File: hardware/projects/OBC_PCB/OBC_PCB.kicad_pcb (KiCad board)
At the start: 2 copper layers, 37 x 61 mm, 10 parts, among them J1 503566-2102, J2 DM3CS-SF, J3 USB4720-03-A, U1 MAX-M10S, U2 NPM1300-CAAA-R, U3 BMA400, U4 BMM350, U5 BMP581, U6 nRF54LM20A-PAXX

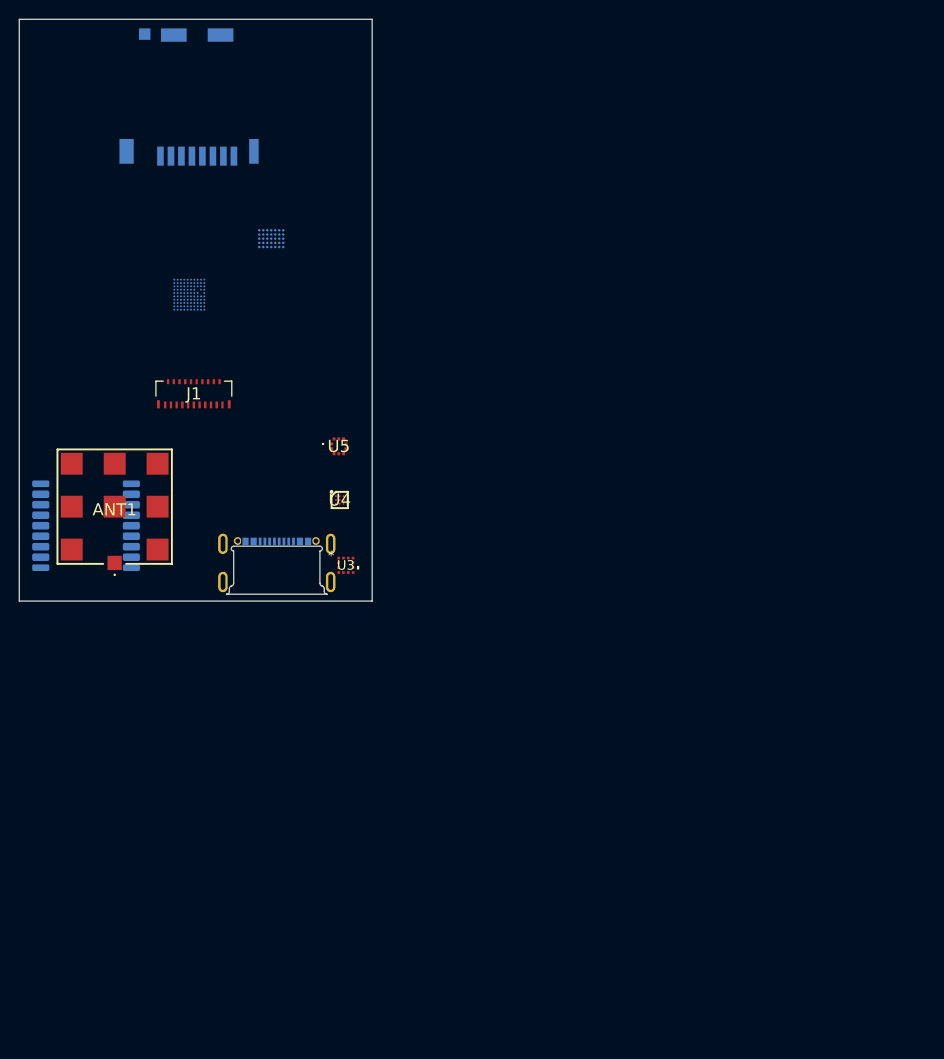
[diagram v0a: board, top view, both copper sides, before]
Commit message: hardware: place components on the enclosure outline and configure HDI rules
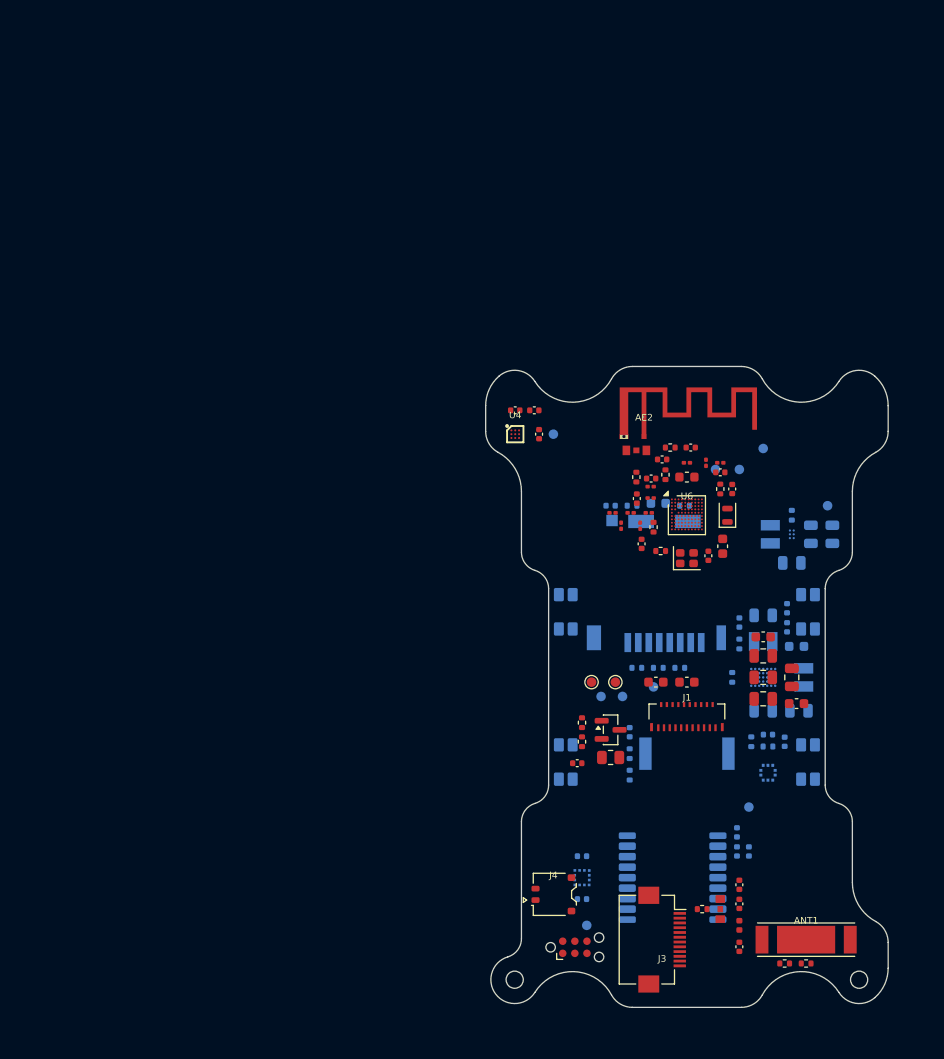
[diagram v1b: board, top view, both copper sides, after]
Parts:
- added AE2: PCB MIFA, RF_Antenna:Texas_SWRA117D_2.4GHz_Right, F.Cu at (95.5, 73.8)
- added BZ1: CPT-9019A-SMT-TR, obc:CPT-9019A-SMT-TR, B.Cu at (100.0, 107.0)
- added C1: 10u, Capacitor_SMD:C_0805_2012Metric, B.Cu at (108.0, 102.5)
- added C10: 10u, Capacitor_SMD:C_0805_2012Metric, B.Cu at (115.2, 84.0)
- added C11: 2.2u, Capacitor_SMD:C_0402_1005Metric, F.Cu at (102.2, 86.2)
- added C12: 4.7u, Capacitor_SMD:C_0201_0603Metric, F.Cu at (100.0, 76.5)
- added C13: 1p, Capacitor_SMD:C_0201_0603Metric, F.Cu at (96.2, 79.0)
- added C14: 1u, Capacitor_SMD:C_0603_1608Metric, F.Cu at (108.0, 94.8)
- added C15: 2.2u, Capacitor_SMD:C_0603_1608Metric, F.Cu at (111.5, 101.8)
- added C16: 100n, Capacitor_SMD:C_0402_1005Metric, B.Cu at (105.5, 93.2)
- added C17: 100n, Capacitor_SMD:C_0402_1005Metric, B.Cu at (110.5, 91.8)
- added C18: 10u, Capacitor_SMD:C_0805_2012Metric, F.Cu at (108.0, 96.8)
- added C19: 10u, Capacitor_SMD:C_0805_2012Metric, F.Cu at (111.0, 99.0)
- added C2: 10u, Capacitor_SMD:C_0805_2012Metric, B.Cu at (111.8, 102.5)
- added C20: 1u, Capacitor_SMD:C_0603_1608Metric, B.Cu at (111.5, 95.8)
- added C21: 10u, Capacitor_SMD:C_0402_1005Metric, F.Cu at (104.8, 79.2)
- added C22: 100n, Capacitor_SMD:C_0402_1005Metric, F.Cu at (94.8, 80.2)
- added C23: 100n, Capacitor_SMD:C_0402_1005Metric, F.Cu at (95.2, 85.0)
- added C24: 100n, Capacitor_SMD:C_0402_1005Metric, F.Cu at (96.2, 78.2)
- added C25: 2.2u, Capacitor_SMD:C_0201_0603Metric, F.Cu at (103.5, 76.5)
- added C26: 4.7u, Capacitor_SMD:C_0402_1005Metric, F.Cu at (103.5, 77.5)
- added C27: 10p, Capacitor_SMD:C_0402_1005Metric, F.Cu at (105.5, 127.2)
- added C28: 2.2u, Capacitor_SMD:C_0402_1005Metric, B.Cu at (105.2, 117.2)
- added C29: 100n, Capacitor_SMD:C_0402_1005Metric, B.Cu at (105.2, 115.2)
- added C3: 10u, Capacitor_SMD:C_0805_2012Metric, B.Cu at (108.0, 92.5)
- added C30: 100n, Capacitor_SMD:C_0402_1005Metric, B.Cu at (106.5, 117.2)
- added C31: 47p, Capacitor_SMD:C_0402_1005Metric, F.Cu at (105.5, 122.8)
- added C32: 4.3p, Capacitor_SMD:C_0402_1005Metric, F.Cu at (105.5, 120.8)
- added C33: 100n, Capacitor_SMD:C_0402_1005Metric, B.Cu at (89.0, 122.2)
- added C34: 100n, Capacitor_SMD:C_0402_1005Metric, B.Cu at (89.0, 117.8)
- added C35: 100n, Capacitor_SMD:C_0402_1005Metric, B.Cu at (110.2, 105.8)
- added C36: 100n, Capacitor_SMD:C_0402_1005Metric, B.Cu at (108.5, 105.0)
- added C37: 100n, Capacitor_SMD:C_0402_1005Metric, F.Cu at (82.0, 71.0)
- added C38: 100n, Capacitor_SMD:C_0402_1005Metric, F.Cu at (84.5, 73.5)
- added C39: 2.2u, Capacitor_SMD:C_0603_1608Metric, F.Cu at (100.0, 99.5)
- added C4: 10u, Capacitor_SMD:C_0805_2012Metric, F.Cu at (108.0, 99.0)
- added C40: 2.2u, Capacitor_SMD:C_0603_1608Metric, F.Cu at (96.8, 99.5)
- added C41: 10u, Capacitor_SMD:C_0603_1608Metric, B.Cu at (97.0, 80.8)
- added C42: 2.2u, Capacitor_SMD:C_0402_1005Metric, F.Cu at (84.0, 71.0)
- added C43: 100n, Capacitor_SMD:C_0402_1005Metric, B.Cu at (92.0, 81.0)
- added C44: 1u, Capacitor_SMD:C_0402_1005Metric, B.Cu at (94.0, 104.8)
- added C45: 1.2p, Capacitor_SMD:C_0201_0603Metric, F.Cu at (95.1, 83.1)
- added C46: 1.5p, Capacitor_SMD:C_0201_0603Metric, F.Cu at (93.1, 83.1)
- added C47: DNP, Capacitor_SMD:C_0402_1005Metric, F.Cu at (97.4, 76.2)
- added C48: DNP, Capacitor_SMD:C_0402_1005Metric, F.Cu at (100.4, 74.9)
- added C49: 1u, Capacitor_SMD:C_0402_1005Metric, F.Cu at (88.5, 108.0)
- added C5: 10u, Capacitor_SMD:C_0805_2012Metric, F.Cu at (108.0, 101.2)
- added C6: 1u, Capacitor_SMD:C_0603_1608Metric, F.Cu at (103.8, 85.2)
- added C7: 100n, Capacitor_SMD:C_0402_1005Metric, B.Cu at (110.5, 93.8)
- added C8: 10u, Capacitor_SMD:C_0805_2012Metric, B.Cu at (113.0, 84.0)
- added C9: 10u, Capacitor_SMD:C_0805_2012Metric, B.Cu at (111.0, 87.0)
- added H1: 1.8mm NPTH, , F.Cu at (81.9, 130.7)
- added H2: 1.8mm NPTH, , F.Cu at (118.1, 130.7)
- added H3: Cradle 4.2x1.6mm NPTH, , F.Cu at (89.0, 114.0)
- added H4: Cradle 4.2x1.6mm NPTH, , F.Cu at (89.0, 78.0)
- added H5: Cradle 4.2x1.6mm NPTH, , F.Cu at (111.0, 114.0)
- added H6: Cradle 4.2x1.6mm NPTH, , F.Cu at (111.0, 78.0)
- added J4: 1S Li-Po, obc:JST_ACH_2pin, F.Cu at (86.0, 121.8)
- added J5: TC2030-CTX-NL, Connector:Tag-Connect_TC2030-IDC-NL_2x03_P1.27mm_Vertical, F.Cu at (88.2, 127.3)
- added J7: RF coax pads, obc:RF_Coax_Solder_GSG, F.Cu at (94.7, 75.2)
- added J8: RF coax pads, obc:RF_Coax_Solder_GSG, F.Cu at (103.5, 123.3)
- added L1: 2.2uH, obc:Wurth_74404024022_2.5x2.0mm, B.Cu at (108.0, 95.2)
- added L10: 3.3nH, Inductor_SMD:L_0201_0603Metric, F.Cu at (92.2, 81.8)
- added L2: 2.2uH, obc:Wurth_74404024022_2.5x2.0mm, B.Cu at (112.2, 99.0)
- added L3: 4.7uH, Inductor_SMD:L_0603_1608Metric, F.Cu at (100.0, 78.0)
- added L4: 120R, Inductor_SMD:L_0201_0603Metric, F.Cu at (102.0, 76.5)
- added L5: 2.2uH, obc:Wurth_74404024022_2.5x2.0mm, B.Cu at (108.8, 84.0)
- added L6: 1.0nH, Inductor_SMD:L_0201_0603Metric, F.Cu at (96.2, 80.2)
- added L7: 3.9nH, Inductor_SMD:L_0402_1005Metric, F.Cu at (105.5, 125.0)
- added L8: 3.6nH, Inductor_SMD:L_0201_0603Metric, F.Cu at (96.0, 81.8)
- added L9: 4.7nH, Inductor_SMD:L_0201_0603Metric, F.Cu at (94.1, 81.8)
- added Q1: AO3400A, Package_TO_SOT_SMD:SOT-23, F.Cu at (92.0, 104.5)
- added R1: 0R, Resistor_SMD:R_0402_1005Metric, B.Cu at (104.8, 99.0)
- added R2: 150k, Resistor_SMD:R_0402_1005Metric, B.Cu at (105.5, 95.5)
- added R20: 10k, Resistor_SMD:R_0402_1005Metric, F.Cu at (97.8, 77.8)
- added R23: 4.7k, Resistor_SMD:R_0402_1005Metric, B.Cu at (108.5, 106.2)
- added R24: 4.7k, Resistor_SMD:R_0402_1005Metric, B.Cu at (106.8, 105.8)
- added R26: 0R, Resistor_SMD:R_0402_1005Metric, F.Cu at (112.5, 129.0)
- added R27: 0R, Resistor_SMD:R_0402_1005Metric, F.Cu at (110.2, 129.0)
- added R28: 47k, Resistor_SMD:R_0402_1005Metric, B.Cu at (94.2, 81.0)
- added R29: 47k, Resistor_SMD:R_0402_1005Metric, B.Cu at (99.8, 81.0)
- added R3: 1M, Resistor_SMD:R_0402_1005Metric, B.Cu at (111.0, 82.0)
- added R30: 47k, Resistor_SMD:R_0402_1005Metric, B.Cu at (97.0, 98.0)
- added R31: 47k, Resistor_SMD:R_0402_1005Metric, B.Cu at (94.8, 98.0)
- added R32: 47k, Resistor_SMD:R_0402_1005Metric, B.Cu at (99.2, 98.0)
- added R33: 1k, Resistor_SMD:R_0402_1005Metric, B.Cu at (94.0, 107.0)
- added R34: 100k, Resistor_SMD:R_0402_1005Metric, B.Cu at (94.0, 109.2)
- added R35: 0R, Resistor_SMD:R_0402_1005Metric, F.Cu at (98.2, 74.9)
- added R36: 220R, Resistor_SMD:R_0805_2012Metric, F.Cu at (92.0, 107.4)
- added R37: 1k, Resistor_SMD:R_0402_1005Metric, F.Cu at (89.0, 103.8)
- added R38: 100k, Resistor_SMD:R_0402_1005Metric, F.Cu at (89.0, 105.8)
- added R39: 0R, Resistor_SMD:R_0402_1005Metric, F.Cu at (94.7, 78.0)
- added R4: 200R, Resistor_SMD:R_0402_1005Metric, F.Cu at (96.5, 83.2)
- added R40: 0R, Resistor_SMD:R_0402_1005Metric, F.Cu at (101.6, 123.3)
- added R5: 2.2R, Resistor_SMD:R_0402_1005Metric, F.Cu at (103.5, 79.2)
- added R9: 33R, Resistor_SMD:R_0402_1005Metric, F.Cu at (97.2, 85.8)
- added SW1: PREV, obc:TL1016AAF220QG, B.Cu at (87.3, 92.1)
- added SW2: NEXT, obc:TL1016AAF220QG, B.Cu at (87.3, 107.9)
- added SW3: SELECT / POWER, obc:TL1016AAF220QG, B.Cu at (112.7, 92.1)
- added SW4: BACK, obc:TL1016AAF220QG, B.Cu at (112.7, 107.9)
- added TP1: SHPHLD, TestPoint:TestPoint_Pad_D1.0mm, B.Cu at (91.0, 101.0)
- added TP10: +5V_DISP, TestPoint:TestPoint_Pad_D1.0mm, B.Cu at (114.8, 81.0)
- added TP11: SCL, TestPoint:TestPoint_Pad_D1.0mm, F.Cu at (90.0, 99.5)
- added TP12: SDA, TestPoint:TestPoint_Pad_D1.0mm, F.Cu at (92.5, 99.5)
- added TP2: SAFEBOOT, TestPoint:TestPoint_Pad_D1.0mm, B.Cu at (93.2, 101.0)
- added TP3: VBAT, TestPoint:TestPoint_Pad_D1.0mm, B.Cu at (89.5, 125.0)
- added TP4: VSYS, TestPoint:TestPoint_Pad_D1.0mm, B.Cu at (108.0, 75.0)
- added TP5: +3V2, TestPoint:TestPoint_Pad_D1.0mm, B.Cu at (103.0, 77.2)
- added TP6: GND, TestPoint:TestPoint_Pad_D1.0mm, B.Cu at (105.5, 77.2)
- added TP7: +3V2_GPS, TestPoint:TestPoint_Pad_D1.0mm, B.Cu at (106.5, 112.6)
- added TP8: +3V3_SD, TestPoint:TestPoint_Pad_D1.0mm, B.Cu at (96.5, 100.0)
- added TP9: +1V8_MAG, TestPoint:TestPoint_Pad_D1.0mm, B.Cu at (86.0, 73.5)
- added U7: TPS610997, obc:TI_YFF0006_0.884x1.226mm_P0.4mm, B.Cu at (111.0, 84.0)
- added Y1: 32MHz, Crystal:Crystal_SMD_2016-4Pin_2.0x1.6mm, F.Cu at (100.0, 86.5)
- added Y3: 32.768kHz, Crystal:Crystal_SMD_2012-2Pin_2.0x1.2mm, F.Cu at (104.2, 82.0)
- ANT1: value SGGP.12.4.A.02 -> GGBLA.125.A; footprint obc:SGGP124A02 -> obc:Taoglas_GGBLA125A_10x3.2mm_ContactPads
- J1: value 503566-2102 -> LS021B7DD02
- J3: value USB4720-03-A -> FH12-12S-0.5SH(55); footprint obc:GCT_USB4720-03-A_REVA -> Connector_FFC-FPC:Hirose_FH12-12S-0.5SH_1x12-1MP_P0.50mm_Horizontal; moved to F.Cu
- U1: value MAX-M10S -> MAX-F11N; footprint RF_GPS:ublox_MAX -> obc:ublox_MAX_F11N_Provisional
- U3, U5: moved to B.Cu
- U6: value nRF54LM20A-PAXX -> nRF54LM20A-PAAA; moved to F.Cu
- moved ANT1 85.5 mm to (112.5, 126.5)
- moved U1 71.7 mm to (98.5, 120.0), turned to 0 degrees
- moved J2 70.7 mm to (97.0, 89.0)
- moved U2 69.1 mm to (108.0, 99.0), turned to 0 degrees
- moved J1 61.8 mm to (100.0, 103.1)
- moved U6 57.0 mm to (100.0, 82.0), turned to 0 degrees
- moved U5 56.5 mm to (108.5, 109.0)
- moved J3 55.1 mm to (97.4, 126.5), turned to -90 degrees
- moved U3 41.1 mm to (89.0, 120.0)
- moved U4 19.7 mm to (82.0, 73.5)
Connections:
- ANT1 pad 1: unconnected-(ANT1-RF_FEED-Pad1) -> Net-(ANT1-~)
- ANT1 pad 2: unconnected-(ANT1-GND-Pad2) -> Net-(ANT1-FTE-Pad2)
- ANT1 pad 3: unconnected-(ANT1-GND-Pad3) -> Net-(ANT1-FTE-Pad3)
- J1 pad 1: unconnected-(J1-Pad1) -> +5V_DISP
- J1 pad 10: unconnected-(J1-Pad10) -> GND
- J1 pad 11: unconnected-(J1-Pad11) -> /Display/LCD.BSP
- J1 pad 12: unconnected-(J1-Pad12) -> /Display/FLPR.P07
- J1 pad 13: unconnected-(J1-Pad13) -> /FLPR.P00
- J1 pad 14: unconnected-(J1-Pad14) -> /FLPR.P04
- J1 pad 15: unconnected-(J1-Pad15) -> /Display/FLPR.P06
- J1 pad 16: unconnected-(J1-Pad16) -> /Display/FLPR.P08
- J1 pad 17: unconnected-(J1-Pad17) -> /Display/FLPR.P09
- J1 pad 18: unconnected-(J1-Pad18) -> /Display/FLPR.P10
- J1 pad 20: unconnected-(J1-Pad20) -> /Display/LCD.VCOM
- J1 pad 3: unconnected-(J1-Pad3) -> /Display/LCD.GSP
- J1 pad 4: unconnected-(J1-Pad4) -> /Display/LCD.GCK
- J1 pad 5: unconnected-(J1-Pad5) -> /Display/LCD.GEN
- J1 pad 6: unconnected-(J1-Pad6) -> /Display/LCD.INTB
- J1 pad 7: unconnected-(J1-Pad7) -> /Display/LCD.VB
- J1 pad 8: unconnected-(J1-Pad8) -> /Display/LCD.VA
- J1 pad 9: unconnected-(J1-Pad9) -> +3V2
- J2 pad 1: unconnected-(J2-DAT2-Pad1) -> /Display/FLPR.P03
- J2 pad 2: unconnected-(J2-CD/DAT3-Pad2) -> /FLPR.P00
- J2 pad 3: unconnected-(J2-CMD-Pad3) -> /Display/FLPR.P05
- J2 pad 4: unconnected-(J2-VDD-Pad4) -> +3V3_SD
- J2 pad 5: unconnected-(J2-CLK-Pad5) -> /Display/FLPR.P01
- J2 pad 6: unconnected-(J2-VSS-Pad6) -> GND
- J2 pad 7: unconnected-(J2-DAT0-Pad7) -> /Display/FLPR.P02
- J2 pad 8: unconnected-(J2-DAT1-Pad8) -> /FLPR.P04
- J2 pad S1: unconnected-(J2-GND-PadS1) -> GND
- J2 pad S2: unconnected-(J2-GND-PadS2) -> GND
- J2 pad S3: unconnected-(J2-GND-PadS3) -> GND
- J2 pad S5: unconnected-(J2-GND-PadS5) -> GND
- U1 pad 1: Net-(U1-GND-Pad1) -> GND
- U1 pad 10: Net-(U1-GND-Pad1) -> GND
- U1 pad 11: unconnected-(U1-RF_IN-Pad11) -> Net-(U1-RF_IN)
- U1 pad 12: Net-(U1-GND-Pad1) -> GND
- U1 pad 18: unconnected-(U1-~{SAFEBOOT}-Pad18) -> Net-(U1-~{SAFEBOOT})
- U1 pad 2: unconnected-(U1-TXD-Pad2) -> /GPS_TXD
- U1 pad 3: unconnected-(U1-RXD-Pad3) -> /GPS_RXD
- U1 pad 6: unconnected-(U1-V_BCKP-Pad6) -> +3V2
- U1 pad 7: unconnected-(U1-VCC_IO-Pad7) -> +3V2_GPS
- U1 pad 8: unconnected-(U1-VCC-Pad8) -> +3V2_GPS
- U2 pad A4: unconnected-(U2-LSOUT1/VOUTLDO1-PadA4) -> +1V8_MAG
- U2 pad A5: unconnected-(U2-LSOUT2/VOUTLDO2-PadA5) -> +3V2_GPS
- U2 pad A6: unconnected-(U2-AVSS-PadA6) -> GND
- U2 pad A7: unconnected-(U2-PVSS1-PadA7) -> GND
- U2 pad B1: unconnected-(U2-VBUS-PadB1) -> VBUS
- U2 pad B2: unconnected-(U2-VBUS-PadB2) -> VBUS
- U2 pad B3: unconnected-(U2-CC2-PadB3) -> /Power Management/USB_CC2
- U2 pad B4: unconnected-(U2-LSIN1/VINLDO1-PadB4) -> +3V2
- U2 pad B5: unconnected-(U2-LSIN2/VINLDO2-PadB5) -> +3V2
- U2 pad B6: unconnected-(U2-VOUT1-PadB6) -> +3V3_SD
- U2 pad B7: unconnected-(U2-SW1-PadB7) -> Net-(U2-SW1)
- U2 pad C1: unconnected-(U2-VSYS-PadC1) -> VSYS
- U2 pad C2: unconnected-(U2-VSYS-PadC2) -> VSYS
- U2 pad C3: unconnected-(U2-VBUSOUT-PadC3) -> USB_VBUS
- U2 pad C6: unconnected-(U2-VOUT2-PadC6) -> +3V2
- U2 pad C7: unconnected-(U2-PVDD-PadC7) -> VSYS
- U2 pad D1: unconnected-(U2-VBAT-PadD1) -> VBAT
- U2 pad D2: unconnected-(U2-VBAT-PadD2) -> VBAT
- U2 pad D3: unconnected-(U2-NTC-PadD3) -> GND
- U2 pad D4: unconnected-(U2-SHPHLD-PadD4) -> /Power Management/SHPHLD
- U2 pad D5: unconnected-(U2-CC1-PadD5) -> /Power Management/USB_CC1
- U2 pad D7: unconnected-(U2-SW2-PadD7) -> Net-(U2-SW2)
- U2 pad E1: unconnected-(U2-VSET2-PadE1) -> Net-(U2-VSET2)
- U2 pad E2: unconnected-(U2-VSET1-PadE2) -> Net-(U2-VSET1)
- U2 pad E3: unconnected-(U2-SCL-PadE3) -> SCL
- U2 pad E4: unconnected-(U2-VDDIO-PadE4) -> +3V2
- U2 pad E5: unconnected-(U2-SDA-PadE5) -> SDA
- U2 pad E6: unconnected-(U2-GPIO1-PadE6) -> PMIC_INT
- U2 pad E7: unconnected-(U2-PVSS2-PadE7) -> GND
- U3 pad 1: unconnected-(U3-SDO-Pad1) -> GND
- U3 pad 10: unconnected-(U3-CSB-Pad10) -> +3V2
- U3 pad 12: unconnected-(U3-SCX-Pad12) -> SCL
- U3 pad 2: unconnected-(U3-SDX-Pad2) -> SDA
- U3 pad 3: unconnected-(U3-VDDIO-Pad3) -> +3V2
- U3 pad 5: unconnected-(U3-INT1-Pad5) -> /ACC_INT1
- U3 pad 7: unconnected-(U3-VDD-Pad7) -> +3V2
- U3 pad 8: unconnected-(U3-GNDIO-Pad8) -> GND
- U3 pad 9: unconnected-(U3-GND-Pad9) -> GND
- U4 pad A2: unconnected-(U4-SDA-PadA2) -> SDA
- U4 pad A3: unconnected-(U4-SCK-PadA3) -> SCL
- U4 pad B1: unconnected-(U4-GND-PadB1) -> GND
- U4 pad B2: unconnected-(U4-ADSEL-PadB2) -> +3V2
- U4 pad B3: unconnected-(U4-VDDIO-PadB3) -> +3V2
- U4 pad C1: unconnected-(U4-VDD-PadC1) -> +1V8_MAG
- U4 pad C2: unconnected-(U4-CRST-PadC2) -> Net-(U4-CRST)
- U4 pad C3: unconnected-(U4-BYPASS-PadC3) -> GND
- U5 pad 1: unconnected-(U5-VDDIO-Pad1) -> +3V2
- U5 pad 10: unconnected-(U5-VDD-Pad10) -> +3V2
- U5 pad 2: unconnected-(U5-SCK-Pad2) -> SCL
- U5 pad 3: unconnected-(U5-VSS-Pad3) -> GND
- U5 pad 4: unconnected-(U5-SDI-Pad4) -> SDA
- U5 pad 5: unconnected-(U5-SDO-Pad5) -> +3V2
- U5 pad 6: unconnected-(U5-CSB-Pad6) -> +3V2
- U5 pad 7: unconnected-(U5-INT-Pad7) -> GND
- U5 pad 8: unconnected-(U5-VSS-Pad8) -> GND
- U5 pad 9: unconnected-(U5-VSS-Pad9) -> GND
- U6 pad A1: Net-(U6A-VSS-PadA1) -> GND
- U6 pad A10: Net-(U6A-VSS-PadA1) -> GND
- U6 pad A2: unconnected-(U6A-XC1-PadA2) -> Net-(U6A-XC1)
- U6 pad A3: Net-(U6A-VDD-PadA3) -> +3V2
- U6 pad A4: Net-(U6A-VDD-PadA3) -> +3V2
- U6 pad A5: unconnected-(U6A-DCC-PadA5) -> Net-(U6A-DCC)
- U6 pad A6: unconnected-(U6A-DECD-PadA6) -> Net-(U6A-DECD)
- U6 pad A7: Net-(U6A-VSS-PadA1) -> GND
- U6 pad A8: unconnected-(U6A-DECA-PadA8) -> Net-(U6A-DECA)
- U6 pad A9: Net-(U6A-VDD-PadA3) -> +3V2
- U6 pad B1: unconnected-(U6A-XC2-PadB1) -> Net-(U6A-XC2)
- U6 pad B10: unconnected-(U6D-P2.00-PadB10) -> /FLPR.P00
- U6 pad B2: unconnected-(U6C-P1.15-PadB2) -> /Display/LCD.VCOM
- U6 pad B3: unconnected-(U6C-P1.16-PadB3) -> /Display/LCD.VB
- U6 pad B4: unconnected-(U6C-P1.17-PadB4) -> /Display/LCD.VA
- U6 pad B9: unconnected-(U6D-P2.06-PadB9) -> /Display/FLPR.P06
- U6 pad C1: unconnected-(U6A-DECRF-PadC1) -> Net-(U6A-DECRF)
- U6 pad C10: unconnected-(U6D-P2.01-PadC10) -> Net-(U6D-P2.01)
- U6 pad C2: unconnected-(U6C-P1.14-PadC2) -> /Display/LCD.BSP
- U6 pad C3: unconnected-(U6C-P1.13-PadC3) -> /Display/LCD.INTB
- U6 pad C4: unconnected-(U6C-P1.12-PadC4) -> /Display/LCD.GEN
- U6 pad C5: unconnected-(U6C-P1.11-PadC5) -> /Display/LCD.GCK
- U6 pad C6: unconnected-(U6A-P1.20-PadC6) -> Net-(U6A-P1.20)
- U6 pad C7: unconnected-(U6A-P1.21-PadC7) -> Net-(U6A-P1.21)
- U6 pad C9: unconnected-(U6D-P2.07-PadC9) -> /Display/FLPR.P07
- U6 pad D1: Net-(U6A-VSS-PadA1) -> GND
- U6 pad D10: unconnected-(U6D-P2.02-PadD10) -> /Display/FLPR.P02
- U6 pad D2: Net-(U6A-VSS-PadA1) -> GND
- U6 pad D4: unconnected-(U6E-P3.12-PadD4) -> Net-(U6E-P3.12)
- U6 pad D5: unconnected-(U6C-P1.10-PadD5) -> /Display/LCD.GSP
- U6 pad D9: unconnected-(U6D-P2.08-PadD9) -> /Display/FLPR.P08
- U6 pad E1: unconnected-(U6A-ANT-PadE1) -> /Radio/ANT
- U6 pad E10: unconnected-(U6D-P2.03-PadE10) -> /Display/FLPR.P03
- U6 pad E3: unconnected-(U6B-P0.09-PadE3) -> /GPS_RXD
- U6 pad E4: unconnected-(U6E-P3.11-PadE4) -> /BACKLIGHT_PWM
- U6 pad E5: Net-(U6A-VSS-PadA1) -> GND
- U6 pad E6: Net-(U6A-VSS-PadA1) -> GND
- U6 pad E9: unconnected-(U6D-P2.09-PadE9) -> /Display/FLPR.P09
- U6 pad F1: Net-(U6A-VSS-PadA1) -> GND
- U6 pad F10: unconnected-(U6D-P2.04-PadF10) -> /FLPR.P04
- U6 pad F2: unconnected-(U6A-~{RESET}-PadF2) -> /nRESET
- U6 pad F3: unconnected-(U6B-P0.08-PadF3) -> PMIC_INT
- U6 pad F5: Net-(U6A-VSS-PadA1) -> GND
- U6 pad F6: Net-(U6A-VSS-PadA1) -> GND
- U6 pad F7: unconnected-(U6E-P3.09-PadF7) -> DISP_5V_EN
- U6 pad F9: unconnected-(U6D-P2.10-PadF9) -> /Display/FLPR.P10
- U6 pad G1: unconnected-(U6A-SWDCLK-PadG1) -> /SWDCLK
- U6 pad G10: Net-(U6A-VDD-PadA3) -> +3V2
- U6 pad G2: unconnected-(U6A-SWDIO-PadG2) -> /SWDIO
- U6 pad G3: unconnected-(U6B-P0.07-PadG3) -> /BTN_BACK
- U6 pad G9: unconnected-(U6D-P2.05-PadG9) -> /Display/FLPR.P05
- U6 pad H1: Net-(U6A-VDD-PadA3) -> +3V2
- U6 pad H2: unconnected-(U6B-P0.06-PadH2) -> /BTN_NEXT
- U6 pad H3: unconnected-(U6B-P0.05-PadH3) -> /BTN_PREV
- U6 pad J2: unconnected-(U6B-P0.03-PadJ2) -> /GPS_TXD
- U6 pad J3: unconnected-(U6B-P0.02-PadJ3) -> SCL
- U6 pad J5: unconnected-(U6A-TXRTUNE-PadJ5) -> Net-(U6A-TXRTUNE)
- U6 pad K1: Net-(U6A-VSS-PadA1) -> GND
- U6 pad K10: Net-(U6A-VSS-PadA1) -> GND
- U6 pad K2: unconnected-(U6B-P0.01-PadK2) -> SDA
- U6 pad K3: unconnected-(U6B-P0.00-PadK3) -> /ACC_INT1
- U6 pad K4: unconnected-(U6A-D--PadK4) -> /Power Management/USB_D-
- U6 pad K5: unconnected-(U6A-D+-PadK5) -> /Power Management/USB_D+
- U6 pad K6: unconnected-(U6A-DECUSB-PadK6) -> Net-(U6A-DECUSB)
- U6 pad K7: unconnected-(U6A-VBUS-PadK7) -> Net-(U6A-VBUS)
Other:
- board size 37 x 61 mm -> 42.2 x 67.2 mm
- copper layers 2 -> 8
- board text added: "BACKLIGHT: Q1/R36-R38/C49 placed; J6 connector/tail footprint TBD."
- board text added: "BMM350: Bosch guide 3.9 says no ENIG. Confirm compatible PCB finish before fabrication."
- board text added: "CRADLE: H3-H6, 4.2x1.6 NPTH; front supports + release access reserved"
- board text added: "DISPLAY + FLEX PROJECTION"
- board text added: "HDI: tentative 3+2+3; filled/capped microvias. U6 land size needs fab approval. RF 50-ohm / USB 90-ohm: width and gap pending stackup. Green mask >= 0.102mm web."
- board text added: "J5: TC2030-CTX-NL. No paste. Keep 0.508mm from other tracks; clear probe access."
- board text added: "PCBWay HDI / 8 layers / 1.6mm target. Confirm stackup and 0.35mm CSP escape."
- board text added: "PLACEMENT DRAFT - UNROUTED"
- board text added: "RF TEST: remove R39 (BLE) or R40 (GNSS). Center pad in feed; no branch stub."
- board text added: "Rough placement only; battery and RF stackup not finalized."
- board text added: "USB + BATTERY: front access below display. Backlight connector pending."

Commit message: hardware: complete first main-board routing pass
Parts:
- removed C44: 1u, Capacitor_SMD:C_0402_1005Metric
- removed R34: 100k, Resistor_SMD:R_0402_1005Metric
- added C50: DNP, Capacitor_SMD:C_0402_1005Metric, B.Cu at (104.9, 116.2)
- added R41: 470R, Resistor_SMD:R_0402_1005Metric, B.Cu at (94.0, 109.2)
- added TP13: USB_VBUS, TestPoint:TestPoint_Pad_D1.0mm, F.Cu at (110.0, 104.0)
- ANT1: footprint obc:Taoglas_GGBLA125A_10x3.2mm_ContactPads -> obc:Taoglas_GGBLA125A_10x3.2mm_Corner
- C12, C13, C25, C45, C46: footprint Capacitor_SMD:C_0201_0603Metric -> obc:C_Nordic_0201_0603Metric
- C27, C31, C32, L7: moved to B.Cu
- L10, L4, L6, L8, L9: footprint Inductor_SMD:L_0201_0603Metric -> obc:L_Nordic_0201_0603Metric
- R33: value 1k -> 470R
- moved C30 14.9 mm to (91.7, 118.9), turned to 180 degrees
- moved C29 13.8 mm to (91.7, 117.8), turned to 180 degrees
- moved C28 13.6 mm to (91.7, 116.7), turned to 180 degrees
- moved C27 12.5 mm to (111.0, 116.0), turned to 0 degrees
- moved R27 12.0 mm to (105.3, 118.0), turned to 90 degrees
- moved L7 11.3 mm to (113.1, 116.6)
- moved J8 11.2 mm to (106.3, 112.5), turned to 90 degrees
- moved C26 11.0 mm to (102.9, 88.5), turned to -90 degrees
- moved R40 9.80 mm to (106.3, 114.7), turned to 90 degrees
- moved C25 9.66 mm to (96.5, 83.1), turned to -90 degrees
- moved C23 9.60 mm to (104.8, 86.0), turned to -90 degrees
- moved R5 9.28 mm to (104.3, 88.5)
- moved R9 9.04 mm to (106.2, 87.0)
- moved R4 8.72 mm to (101.2, 90.6)
- moved C20 8.11 mm to (105.5, 101.2)
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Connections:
- net PMIC_INT renamed /PMIC_INT
- net USB_VBUS renamed /USB_VBUS
- BZ1 pad 2: GND -> Net-(BZ1-~-Pad2)
- J3 pad 1: VBUS -> GND
- J3 pad 10: /Power Management/USB_CC2 -> VBUS
- J3 pad 11: GND -> VBUS
- J3 pad 4: VBUS -> /Power Management/USB_CC1
- J3 pad 5: /Power Management/USB_CC1 -> GND
- J3 pad 6: GND -> /Power Management/USB_D+
- J3 pad 7: /Power Management/USB_D+ -> /Power Management/USB_D-
- J3 pad 8: /Power Management/USB_D- -> GND
- J3 pad 9: GND -> /Power Management/USB_CC2
- R23 pad 2: SDA -> /SDA
- R24 pad 2: SCL -> /SCL
- R3 pad 1: DISP_5V_EN -> /DISP_5V_EN
- R33 pad 1: Net-(U6E-P3.12) -> /PIEZO_A
- R33 pad 2: Net-(C44-Pad1) -> Net-(BZ1-~-Pad1)
- TP11 pad 1: SCL -> /SCL
- TP12 pad 1: SDA -> /SDA
- U2 pad E3: SCL -> /SCL
- U2 pad E5: SDA -> /SDA
- U3 pad 12: SCL -> /SCL
- U3 pad 2: SDA -> /SDA
- U4 pad A2: SDA -> /SDA
- U4 pad A3: SCL -> /SCL
- U5 pad 2: SCL -> /SCL
- U5 pad 4: SDA -> /SDA
- U5 pad 7: GND -> /BARO_INT
- U6 pad C5: /Display/LCD.GCK -> unconnected-(U6C-P1.11-PadC5)
- U6 pad D4: Net-(U6E-P3.12) -> unconnected-(U6E-P3.12-PadD4)
- U6 pad E4: /BACKLIGHT_PWM -> unconnected-(U6E-P3.11-PadE4)
- U6 pad F7: DISP_5V_EN -> unconnected-(U6E-P3.09-PadF7)
- U6 pad H10: unconnected-(U6C-P1.29-PadH10) -> /DISP_5V_EN
- U6 pad H8: unconnected-(U6C-P1.05-PadH8) -> /Display/LCD.GCK
- U6 pad H9: unconnected-(U6C-P1.03-PadH9) -> /SCL
- U6 pad J10: unconnected-(U6C-P1.30-PadJ10) -> /BACKLIGHT_PWM
- U6 pad J3: SCL -> unconnected-(U6B-P0.02-PadJ3)
- U6 pad J9: unconnected-(U6C-P1.04-PadJ9) -> /SDA
- U6 pad K2: SDA -> /BARO_INT
- U6 pad K8: unconnected-(U6C-P1.00-PadK8) -> /PIEZO_B
- U6 pad K9: unconnected-(U6C-P1.31-PadK9) -> /PIEZO_A
- U7 pad C1: DISP_5V_EN -> /DISP_5V_EN
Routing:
- net /SDA: track 0.00 -> 113.0 mm, vias 0 -> 15
- net /SCL: track 0.00 -> 102.4 mm, vias 0 -> 14
- net +3V3_SD: track 0.00 -> 70.5 mm, vias 0 -> 9
- net /nRESET: track 0.00 -> 67.8 mm, vias 0 -> 5
- net +1V8_MAG: track 0.00 -> 66.0 mm, vias 0 -> 11
- net VBAT: track 0.00 -> 62.6 mm, vias 0 -> 3
- net /PIEZO_A: track 0.00 -> 55.6 mm, vias 0 -> 7
- net +5V_DISP: track 0.00 -> 54.6 mm, vias 0 -> 3
- net /GPS_RXD: track 0.00 -> 51.4 mm, vias 0 -> 3
- net +3V2: track 0.00 -> 50.0 mm, vias 0 -> 48
- net /SWDIO: track 0.00 -> 49.9 mm, vias 0 -> 3
- net /SWDCLK: track 0.00 -> 49.2 mm, vias 0 -> 3
- net /BACKLIGHT_PWM: track 0.00 -> 48.0 mm, vias 0 -> 9
- net /Display/FLPR.P06: track 0.00 -> 47.4 mm, vias 0 -> 4
- net +3V2_GPS: track 0.00 -> 46.0 mm, vias 0 -> 4
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- added copper zone on In3.Cu, net +3V2
- added copper zone on B.Cu, net GND
- added copper zone on F.Cu, net GND
- added copper zone on In1.Cu, net GND
- added copper zone on In4.Cu, net GND
- added copper zone on In6.Cu, net GND

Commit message: hardware: rework main-board routing after layout review
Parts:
- added FID1: Fiducial_1mm_Mask2mm, Fiducial:Fiducial_1mm_Mask2mm, F.Cu at (85.2, 80.5)
- added FID10: Fiducial_0.5mm_Mask1mm, Fiducial:Fiducial_0.5mm_Mask1mm, B.Cu at (110.0, 110.0)
- added FID2: Fiducial_1mm_Mask2mm, Fiducial:Fiducial_1mm_Mask2mm, F.Cu at (114.8, 85.5)
- added FID3: Fiducial_1mm_Mask2mm, Fiducial:Fiducial_1mm_Mask2mm, F.Cu at (95.0, 119.0)
- added FID4: Fiducial_1mm_Mask2mm, Fiducial:Fiducial_1mm_Mask2mm, B.Cu at (85.2, 80.5)
- added FID5: Fiducial_1mm_Mask2mm, Fiducial:Fiducial_1mm_Mask2mm, B.Cu at (107.0, 81.0)
- added FID6: Fiducial_1mm_Mask2mm, Fiducial:Fiducial_1mm_Mask2mm, B.Cu at (85.8, 124.5)
- added FID7: Fiducial_0.5mm_Mask1mm, Fiducial:Fiducial_0.5mm_Mask1mm, F.Cu at (97.2, 89.2)
- added FID8: Fiducial_0.5mm_Mask1mm, Fiducial:Fiducial_0.5mm_Mask1mm, F.Cu at (105.8, 80.8)
- added FID9: Fiducial_0.5mm_Mask1mm, Fiducial:Fiducial_0.5mm_Mask1mm, B.Cu at (106.8, 110.6)
- C14, C15, C18, C19, C4, C5, J8, R40: moved to B.Cu
- R33, R41: moved to F.Cu
- moved C35 32.5 mm to (87.2, 82.8), turned to 0 degrees
- moved U5 31.7 mm to (87.2, 85.5)
- moved TP4 27.2 mm to (101.1, 101.3)
- moved C36 27.1 mm to (87.2, 88.2)
- moved R41 22.9 mm to (102.2, 87.8), turned to -90 degrees
- moved R33 21.5 mm to (104.0, 88.0), turned to -90 degrees
- moved C43 17.6 mm to (99.0, 97.2)
- moved C41 17.4 mm to (97.1, 98.1), turned to -90 degrees
- moved TP7 16.1 mm to (90.6, 110.0), turned to 180 degrees
- moved BZ1 16.0 mm to (99.0, 123.0)
- moved TP2 14.8 mm to (94.0, 115.8)
- moved C28 12.8 mm to (90.5, 104.0)
- moved C29 12.3 mm to (90.5, 105.6)
- moved U1 12.0 mm to (98.0, 108.0)
- moved C30 11.8 mm to (90.5, 107.2)
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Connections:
- net Net-(AE2-FEED) renamed /Radio/RF24_FEED
- net Net-(ANT1-FTE-Pad2) renamed /GNSS/GNSS_FTE1
- net Net-(ANT1-FTE-Pad3) renamed /GNSS/GNSS_FTE2
- net Net-(ANT1-~) renamed /GNSS/GNSS_RF_FEED
- net Net-(C27-Pad1) renamed /GNSS/GNSS_RF_MATCH
- net Net-(C45-Pad1) renamed /Radio/RF24_M1
- net Net-(C46-Pad1) renamed /Radio/RF24_M2
- net Net-(J7-In) renamed /Radio/RF24_TEST
- net Net-(J8-In) renamed /GNSS/GNSS_RF_TEST
- net Net-(L10-Pad2) renamed /Radio/RF24_LPF
- net Net-(U1-RF_IN) renamed /GNSS/GNSS_RF_IN
- net Net-(U2-SW1) renamed /Power Management/PMIC_SW1
- net Net-(U2-SW2) renamed /Power Management/PMIC_SW2
- net Net-(U6A-DCC) renamed /SOC_DCC
- net Net-(U6A-VBUS) renamed /SOC_USB_VBUS
- net Net-(U7-SW) renamed /Power Management/BOOST_SW
- J1 pad MP1: unconnected-(J1-PadMP1) -> GND
- J1 pad MP2: unconnected-(J1-PadMP2) -> GND
- J3 pad MP: (no net) -> GND
- J4 pad MP: (no net) -> GND
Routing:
- net Net-(BZ1-~-Pad1): track 1.86 -> 62.4 mm, vias 0 -> 9
- net /PIEZO_A: track 55.6 -> 3.48 mm, vias 7 -> 0
- net /FLPR.P00: track 33.3 -> 83.7 mm, vias 5 -> 7
- net /Display/FLPR.P10: track 18.8 -> 54.6 mm, vias 2 -> 11
- net /Display/FLPR.P05: track 31.2 -> 66.3 mm, vias 4 -> 14
- net /SCL: track 102.4 -> 136.9 mm, vias 14 -> 32
- net /PIEZO_B: track 33.8 -> 2.33 mm, vias 5 -> 0
- net Net-(BZ1-~-Pad2): track 11.3 -> 40.8 mm, vias 0 -> 2
- net /SDA: track 113.0 -> 141.6 mm, vias 15 -> 36
- net /BARO_INT: track 36.9 -> 13.0 mm
- net /Display/FLPR.P09: track 31.8 -> 53.1 mm, vias 5 -> 11
- net Net-(U1-~{SAFEBOOT}): track 28.9 -> 8.85 mm
- net /Power Management/USB_CC1: track 37.3 -> 57.1 mm, vias 4 -> 8
- net /DISP_5V_EN: track 12.1 -> 31.1 mm, vias 3 -> 5
- net /Display/FLPR.P07: track 31.2 -> 49.7 mm, vias 3 -> 19
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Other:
- board text added: "+"
- board text added: "-"
- board text added: "1V8"
- board text added: "3V2"
- board text added: "BOOT"
- board text added: "DISP 5V"
- board text added: "GND"
- board text added: "GPS 3V2"
- board text added: "OpenBikeComputer"
- board text added: "PROVISIONAL 3+2+3 HDI, 1.6 mm. 35/18 um Cu; 100 um build-up; 802 um core. FR4 Dk 4.2 assumed. Fab to confirm stack, impedance, finish and CSP lands. Filled/capped microvias. RF 50-ohm / USB 90-ohm geometry pending stackup."
- board text added: "Prototype: validate stackup, CSP lands, antenna tuning and mechanical fit."
- board text added: "REV A - PROTOTYPE"
- board text added: "ROUTING PROTOTYPE - NOT FOR FABRICATION"
- board text added: "SCL"
- board text added: "SD 3V3"
- board text added: "SDA"
- board text added: "SHPHLD"
- board text added: "SWD"
- board text added: "USB 5V"
- board text added: "VBAT"
- board text added: "VSYS"
- board text added: "openbikecomputer.com"
- board text removed: "HDI: tentative 3+2+3; filled/capped microvias. U6 land size needs fab approval. RF 50-ohm / USB 90-ohm: width and gap pending stackup. Green mask >= 0.102mm web."
- board text removed: "PLACEMENT DRAFT - UNROUTED"
- board text removed: "Rough placement only; battery and RF stackup not finalized."
